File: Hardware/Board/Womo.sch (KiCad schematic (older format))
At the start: 0 parts

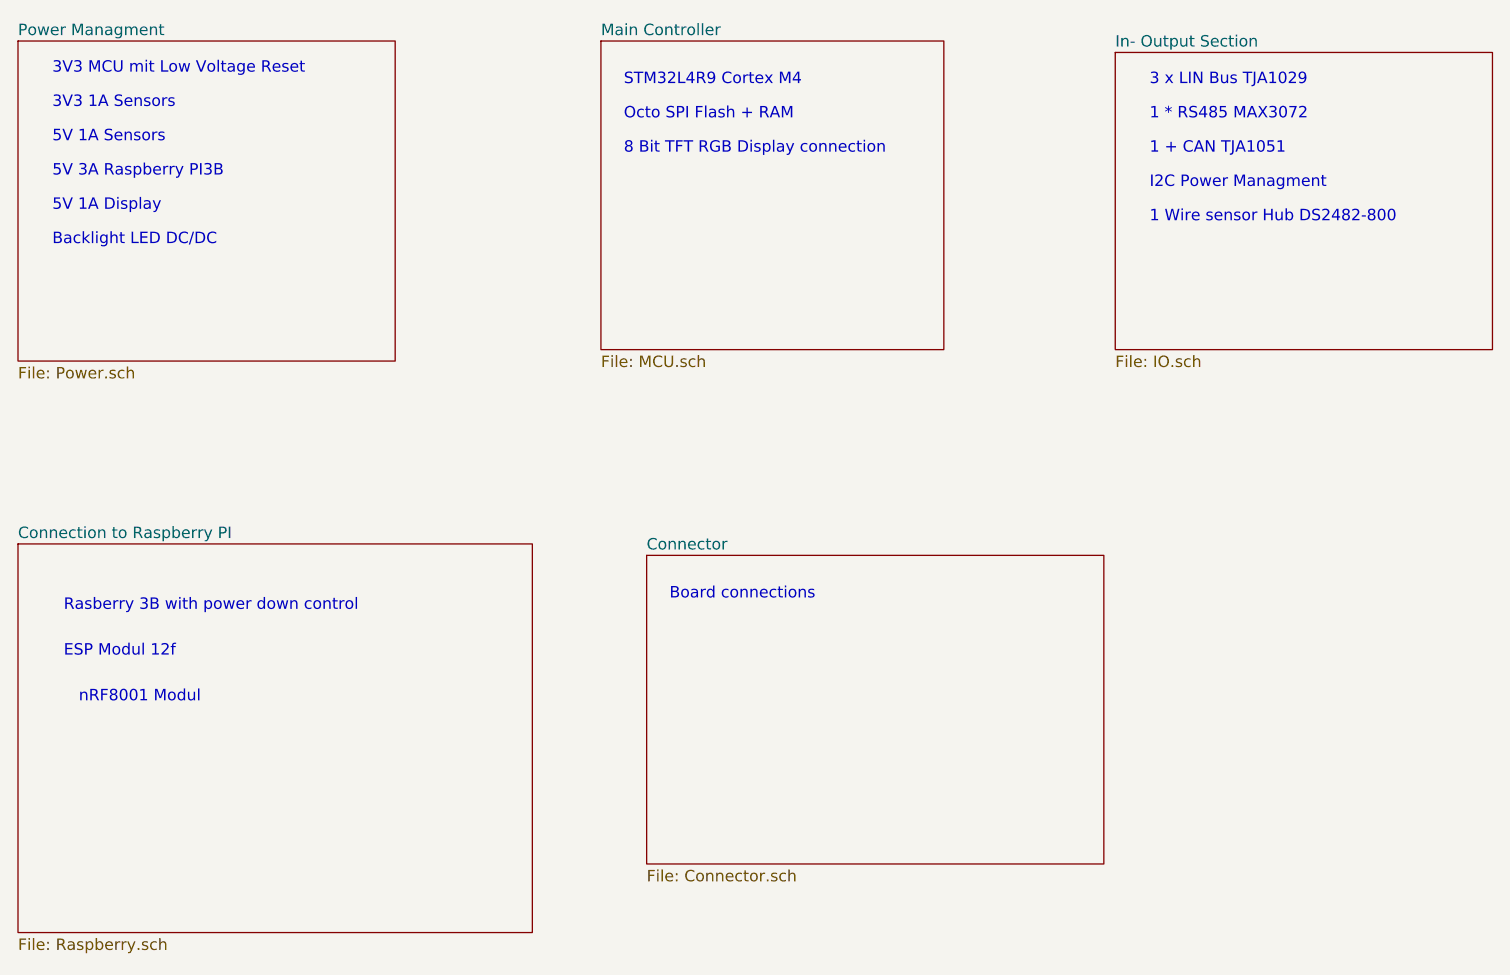
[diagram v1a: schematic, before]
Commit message: Komplete enummerierung Geändert, Schaltplan zusammengefasst, Layout nochmals reset. BOM zu 75% fertig gestellt
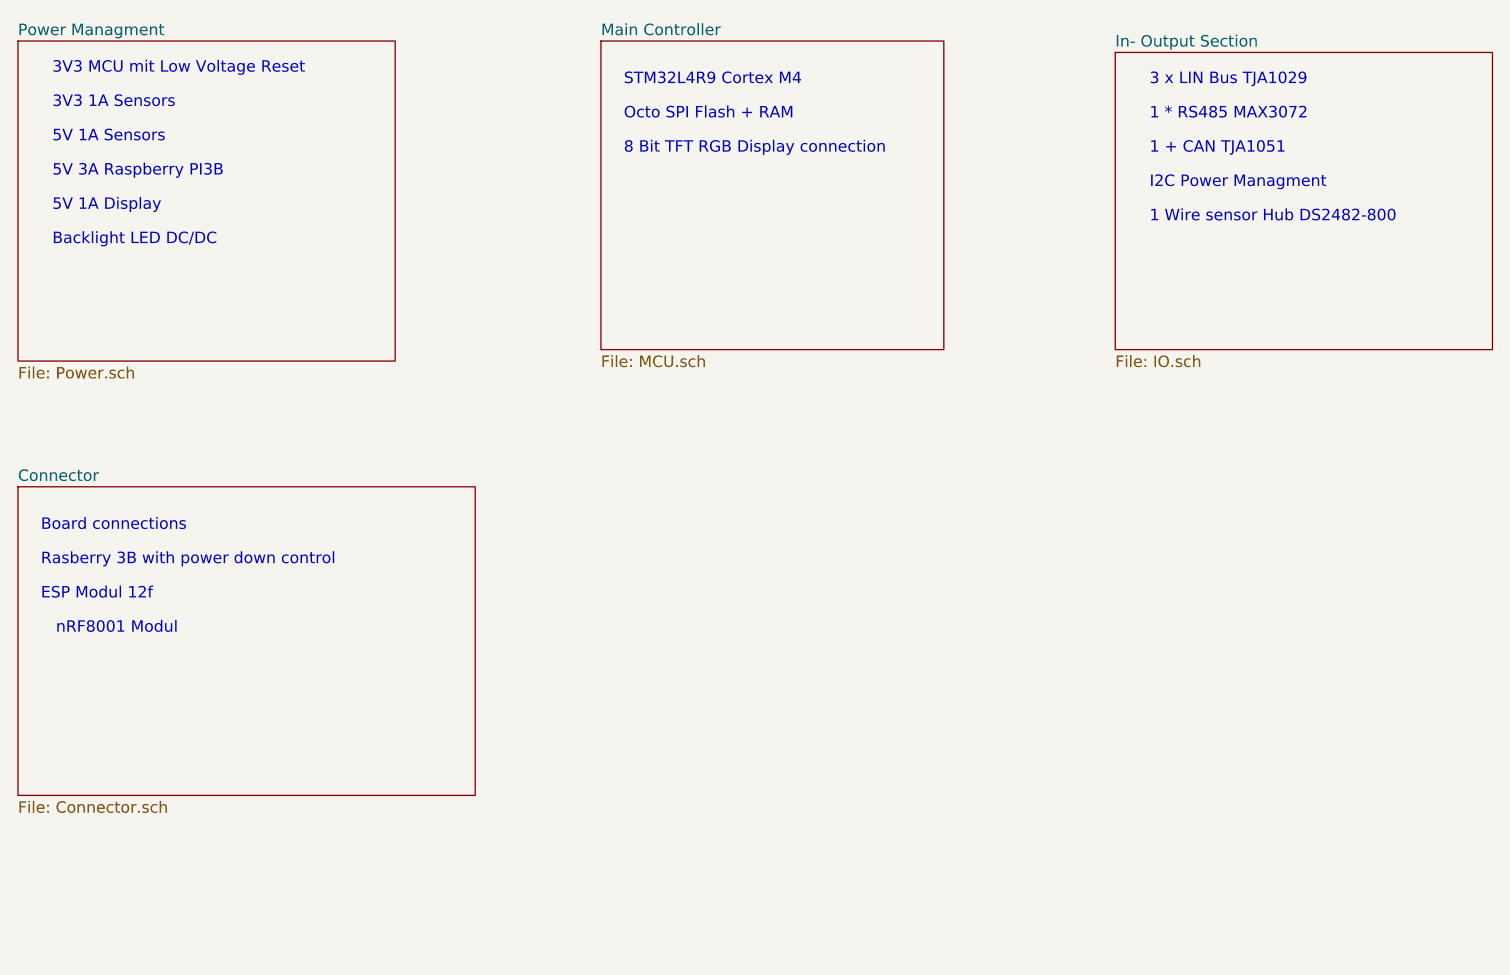
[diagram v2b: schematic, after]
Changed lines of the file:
@@
 EESchema Schematic File Version 4
 LIBS:Womo-cache
-EELAYER 29 0
+EELAYER 26 0
 EELAYER END
 $Descr A4 11693 8268
 encoding utf-8
-Sheet 1 6
+Sheet 1 5
 Title ""
 Date ""
@@
 $EndSheet
 $Sheet
-S 1150 3350 2250 1700
-U 5C8BC88B
-F0 "Connection to Raspberry PI" 50
-F1 "Raspberry.sch" 50
-$EndSheet
-$Sheet
-S 3900 3400 2000 1350
+S 1150 3100 2000 1350
 U 5CC9A992
 F0 "Connector" 50
@@
 Text Notes 6100 1650 0    50   ~ 0
 1 + CAN TJA1051\n
-Text Notes 1350 3650 0    50   ~ 0
+Text Notes 1250 3450 0    50   ~ 0
 Rasberry 3B with power down control
-Text Notes 1350 3850 0    50   ~ 0
+Text Notes 1250 3600 0    50   ~ 0
 ESP Modul 12f
 Text Notes 6100 1950 0    50   ~ 0
 1 Wire sensor Hub DS2482-800
-Text Notes 4000 3600 0    50   ~ 0
+Text Notes 1250 3300 0    50   ~ 0
 Board connections
-Text Notes 1950 4050 2    50   ~ 0
+Text Notes 1850 3750 2    50   ~ 0
 nRF8001 Modul\n
 $Sheet

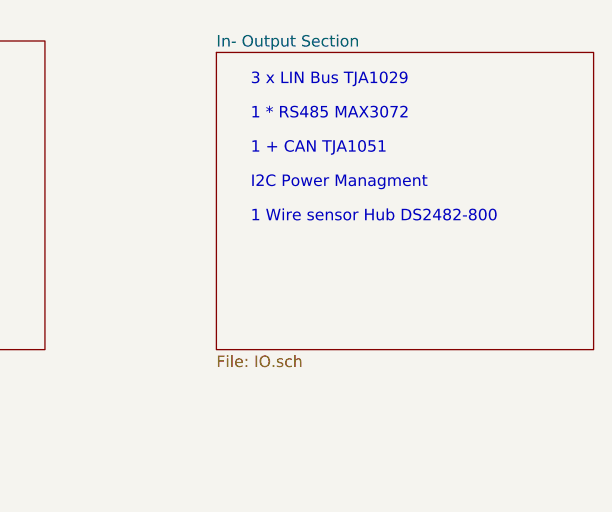
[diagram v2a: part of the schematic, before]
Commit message: Änderung des Konzeptes auf 2 Boards, eines TFT Touch mit STM32L4R9, das rein die Bedienung macht. Control Board mit STM32L476, mit noch mehr Schnittstellen. Bus zwischen Display, Board, Raspberry/ESP ist RS485, Bus als RJ45 mit Wakeup und Stromversorgung
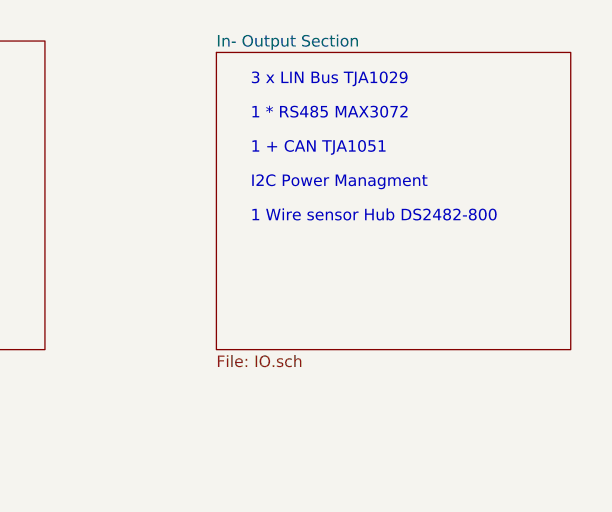
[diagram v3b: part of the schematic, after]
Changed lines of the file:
@@
 $EndDescr
-$Sheet
-S 5950 1200 1650 1300
-U 5C8BBC97
-F0 "In- Output Section" 50
-F1 "IO.sch" 50
-$EndSheet
 $Sheet
 S 1150 1150 1650 1400
@@
 Text Notes 6100 1800 0    50   ~ 0
 I2C Power Managment
+$Sheet
+S 5950 1200 1550 1300
+U 5C8BBC97
+F0 "In- Output Section" 50
+F1 "IO.sch" 50
+$EndSheet
 $EndSCHEMATC

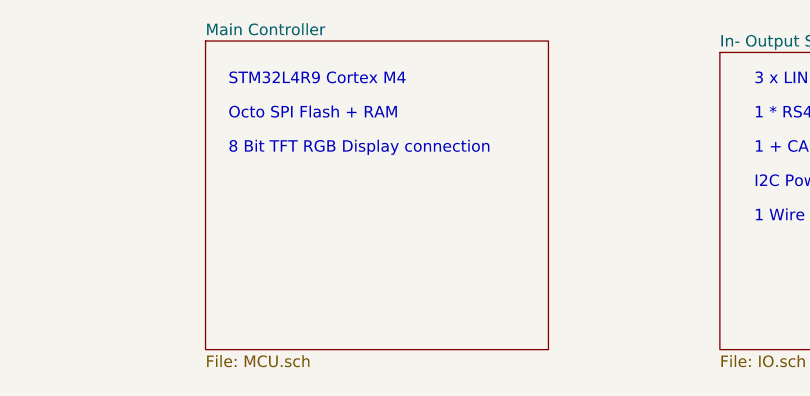
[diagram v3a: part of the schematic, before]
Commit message: Display Unit Lib Fehler behoben, und noch Zeug raus geworfen Library jetzt projekt spezifisch im Hardware root.. Hauptplatine rund um den Prozessor a bissl was getan, vorbereitung Quadspi Flash und SD Karte.
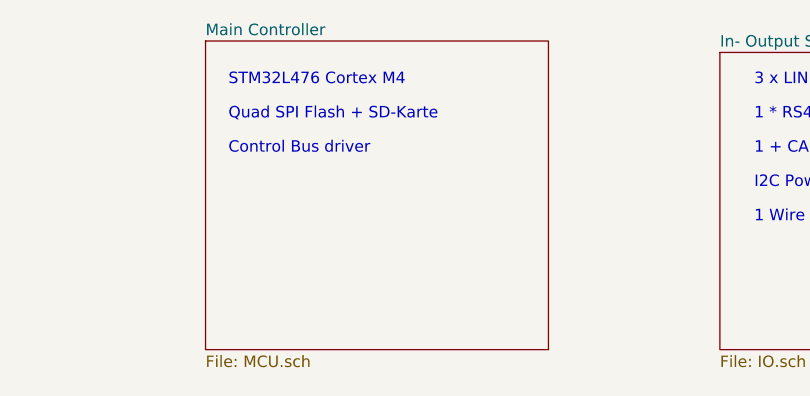
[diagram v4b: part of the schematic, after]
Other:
- note added: "Control Bus driver\n"
- note added: "Quad SPI Flash + SD-Karte\n"
- note added: "STM32L476 Cortex M4\n"
- note removed: "8 Bit TFT RGB Display connection\n"
- note removed: "Octo SPI Flash + RAM\n"
- note removed: "STM32L4R9 Cortex M4\n"
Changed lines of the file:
@@
 5V 1A Display
 Text Notes 3800 1350 0    50   ~ 0
-STM32L4R9 Cortex M4\n
+STM32L476 Cortex M4\n
 Text Notes 3800 1500 0    50   ~ 0
-Octo SPI Flash + RAM\n
+Quad SPI Flash + SD-Karte\n
 Text Notes 3800 1650 0    50   ~ 0
-8 Bit TFT RGB Display connection\n
+Control Bus driver\n
 Text Notes 6100 1350 0    50   ~ 0
 3 x LIN Bus TJA1029\n

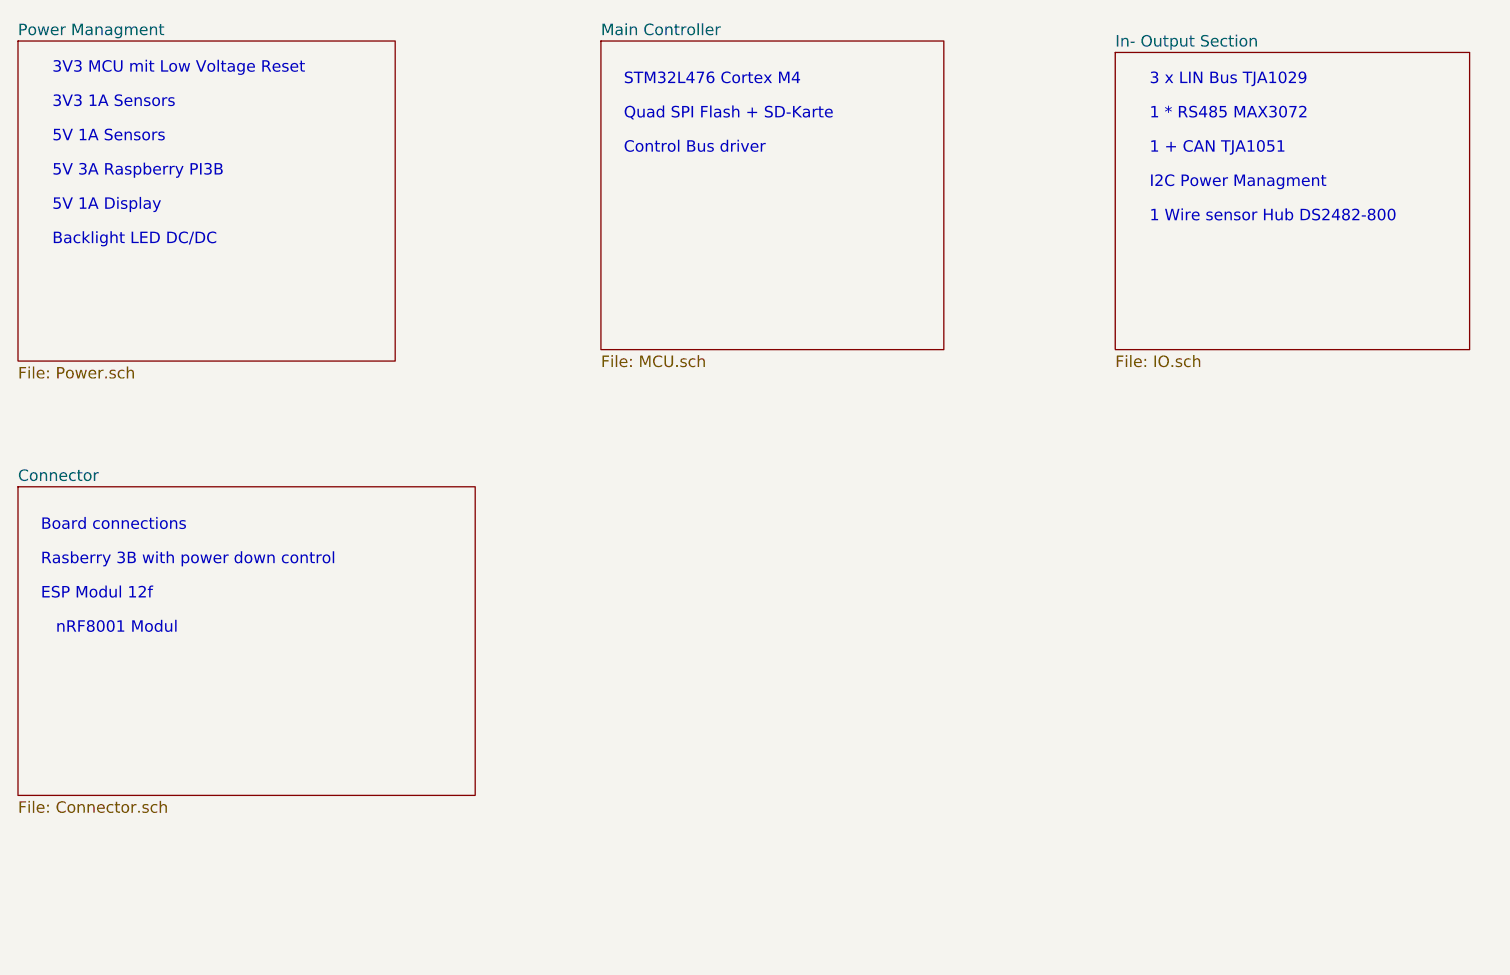
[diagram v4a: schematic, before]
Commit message: Alle Busse aus dem Prozessor geroutet, Multplexing der LIN, RS485 und TTY Busse, diverse Aufräumarbeiten.
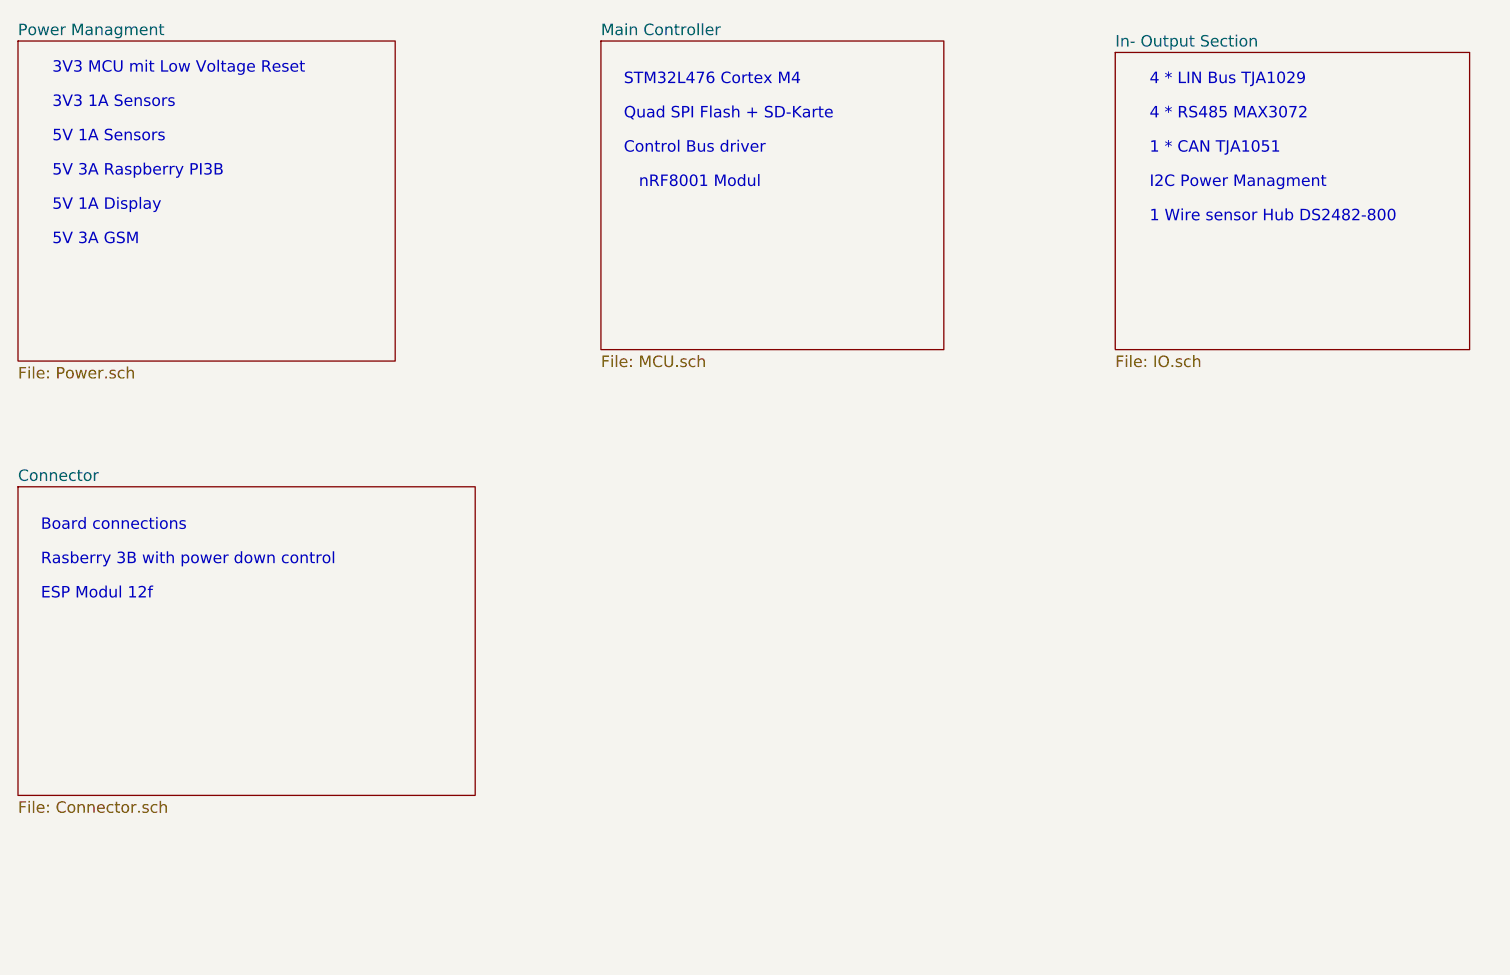
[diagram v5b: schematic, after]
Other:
- note added: "1 * CAN TJA1051\n"
- note added: "4 * LIN Bus TJA1029\n"
- note added: "4 * RS485 MAX3072\n"
- note added: "5V 3A GSM"
- note removed: "1 * RS485 MAX3072\n"
- note removed: "1 + CAN TJA1051\n"
- note removed: "3 x LIN Bus TJA1029\n"
- note removed: "Backlight LED DC/DC"
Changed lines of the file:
@@
 Control Bus driver\n
 Text Notes 6100 1350 0    50   ~ 0
-3 x LIN Bus TJA1029\n
+4 * LIN Bus TJA1029\n
 Text Notes 6100 1500 0    50   ~ 0
-1 * RS485 MAX3072\n
+4 * RS485 MAX3072\n
 Text Notes 6100 1650 0    50   ~ 0
-1 + CAN TJA1051\n
+1 * CAN TJA1051\n
 Text Notes 1250 3450 0    50   ~ 0
 Rasberry 3B with power down control
@@
 Text Notes 1250 3300 0    50   ~ 0
 Board connections
-Text Notes 1850 3750 2    50   ~ 0
+Text Notes 4400 1800 2    50   ~ 0
 nRF8001 Modul\n
 $Sheet
@@
 $EndSheet
 Text Notes 1300 2050 0    50   ~ 0
-Backlight LED DC/DC
+5V 3A GSM
 Text Notes 6100 1800 0    50   ~ 0
 I2C Power Managment

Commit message: Schaltplan erst mal fertig gestellt, Bilblotheken angepasst, High Side Treiber zugefügt
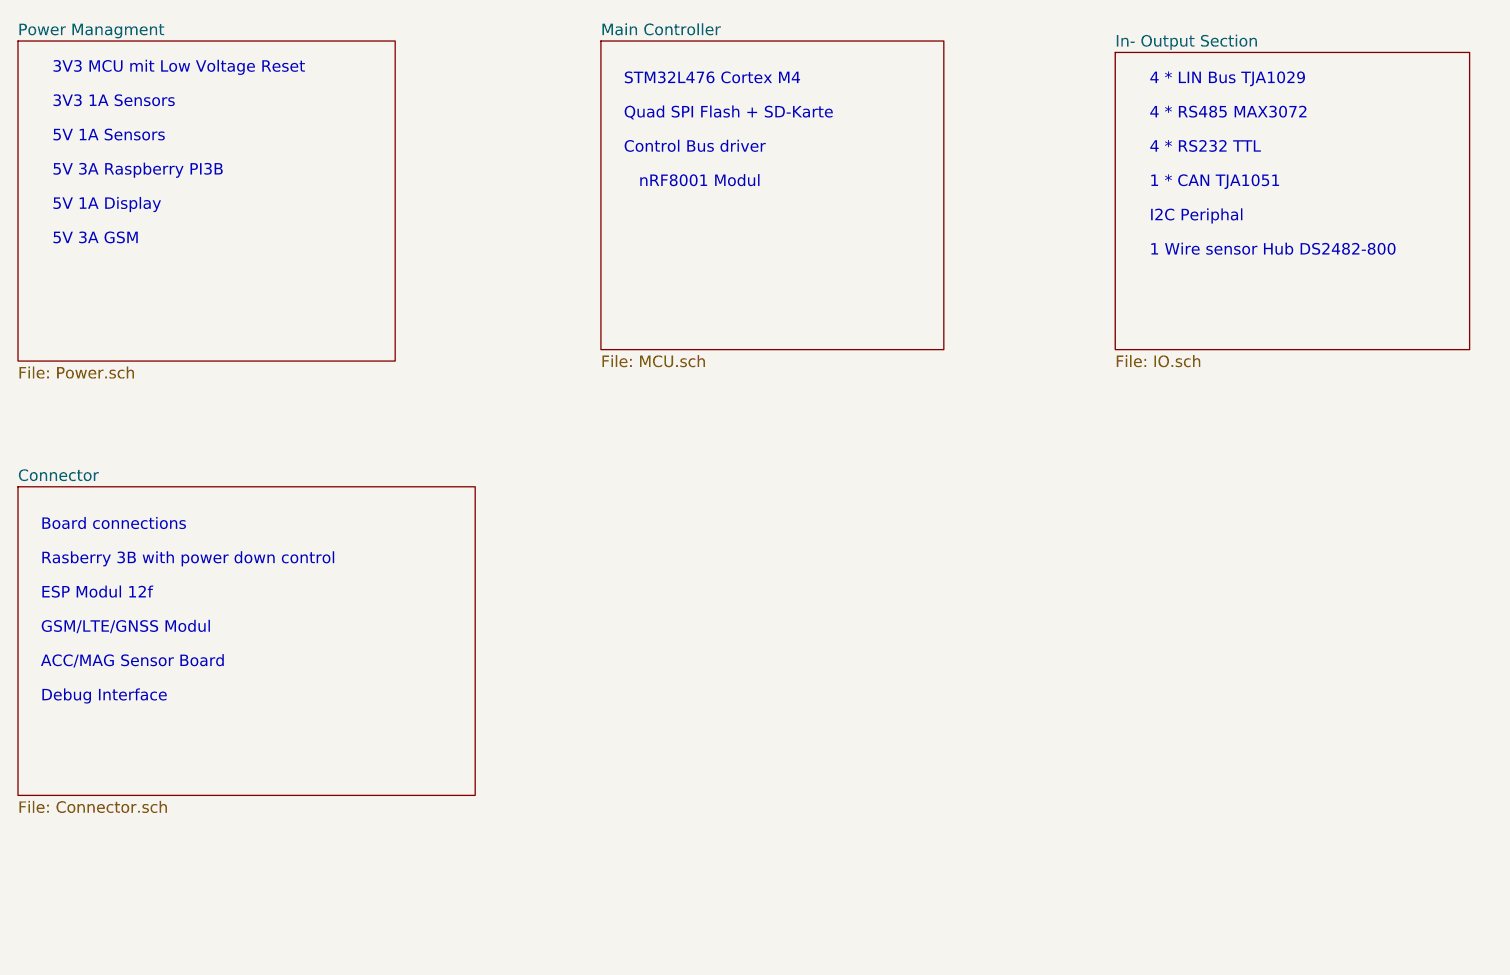
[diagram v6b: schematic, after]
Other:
- note added: "4 * RS232 TTL\n"
- note added: "ACC/MAG Sensor Board"
- note added: "Debug Interface"
- note added: "GSM/LTE/GNSS Modul\n"
- note added: "I2C Periphal"
- note removed: "I2C Power Managment"
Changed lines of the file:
@@
 Text Notes 6100 1350 0    50   ~ 0
 4 * LIN Bus TJA1029\n
-Text Notes 6100 1500 0    50   ~ 0
-4 * RS485 MAX3072\n
 Text Notes 6100 1650 0    50   ~ 0
+4 * RS232 TTL\n
+Text Notes 6100 1800 0    50   ~ 0
 1 * CAN TJA1051\n
 Text Notes 1250 3450 0    50   ~ 0
 Rasberry 3B with power down control
-Text Notes 1250 3600 0    50   ~ 0
-ESP Modul 12f
-Text Notes 6100 1950 0    50   ~ 0
+Text Notes 1250 4050 0    50   ~ 0
+Debug Interface
+Text Notes 6100 2100 0    50   ~ 0
 1 Wire sensor Hub DS2482-800
 Text Notes 1250 3300 0    50   ~ 0
@@
 Text Notes 1300 2050 0    50   ~ 0
 5V 3A GSM
-Text Notes 6100 1800 0    50   ~ 0
-I2C Power Managment
+Text Notes 6100 1950 0    50   ~ 0
+I2C Periphal
 $Sheet
 S 5950 1200 1550 1300
@@
 F1 "IO.sch" 50
 $EndSheet
+Text Notes 1250 3600 0    50   ~ 0
+ESP Modul 12f
+Text Notes 1250 3750 0    50   ~ 0
+GSM/LTE/GNSS Modul\n
+Text Notes 1250 3900 0    50   ~ 0
+ACC/MAG Sensor Board
+Text Notes 6100 1500 0    50   ~ 0
+4 * RS485 MAX3072\n
 $EndSCHEMATC
